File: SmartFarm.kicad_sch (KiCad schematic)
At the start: 30 parts, among them J1 Conn_01x20_Pin, J10 Conn_01x06_Socket, J11 Conn_01x06_Socket, J12 Conn_01x01_Pin, J13 Conn_01x01_Pin, J14 Conn_01x01_Pin, J15 Conn_01x01_Pin, J2 Conn_01x20_Pin, J3 Conn_01x06_Socket, J4 Conn_01x04, J5 Screw_Terminal_01x03, J6 Conn_01x01_Pin, J7 Screw_Terminal_01x03, J8 Barrel_Jack, J9 Screw_Terminal_01x03, SW1 SW_DIP_x01, SW2 SW_MEC_5E, SW3 SW_MEC_5E

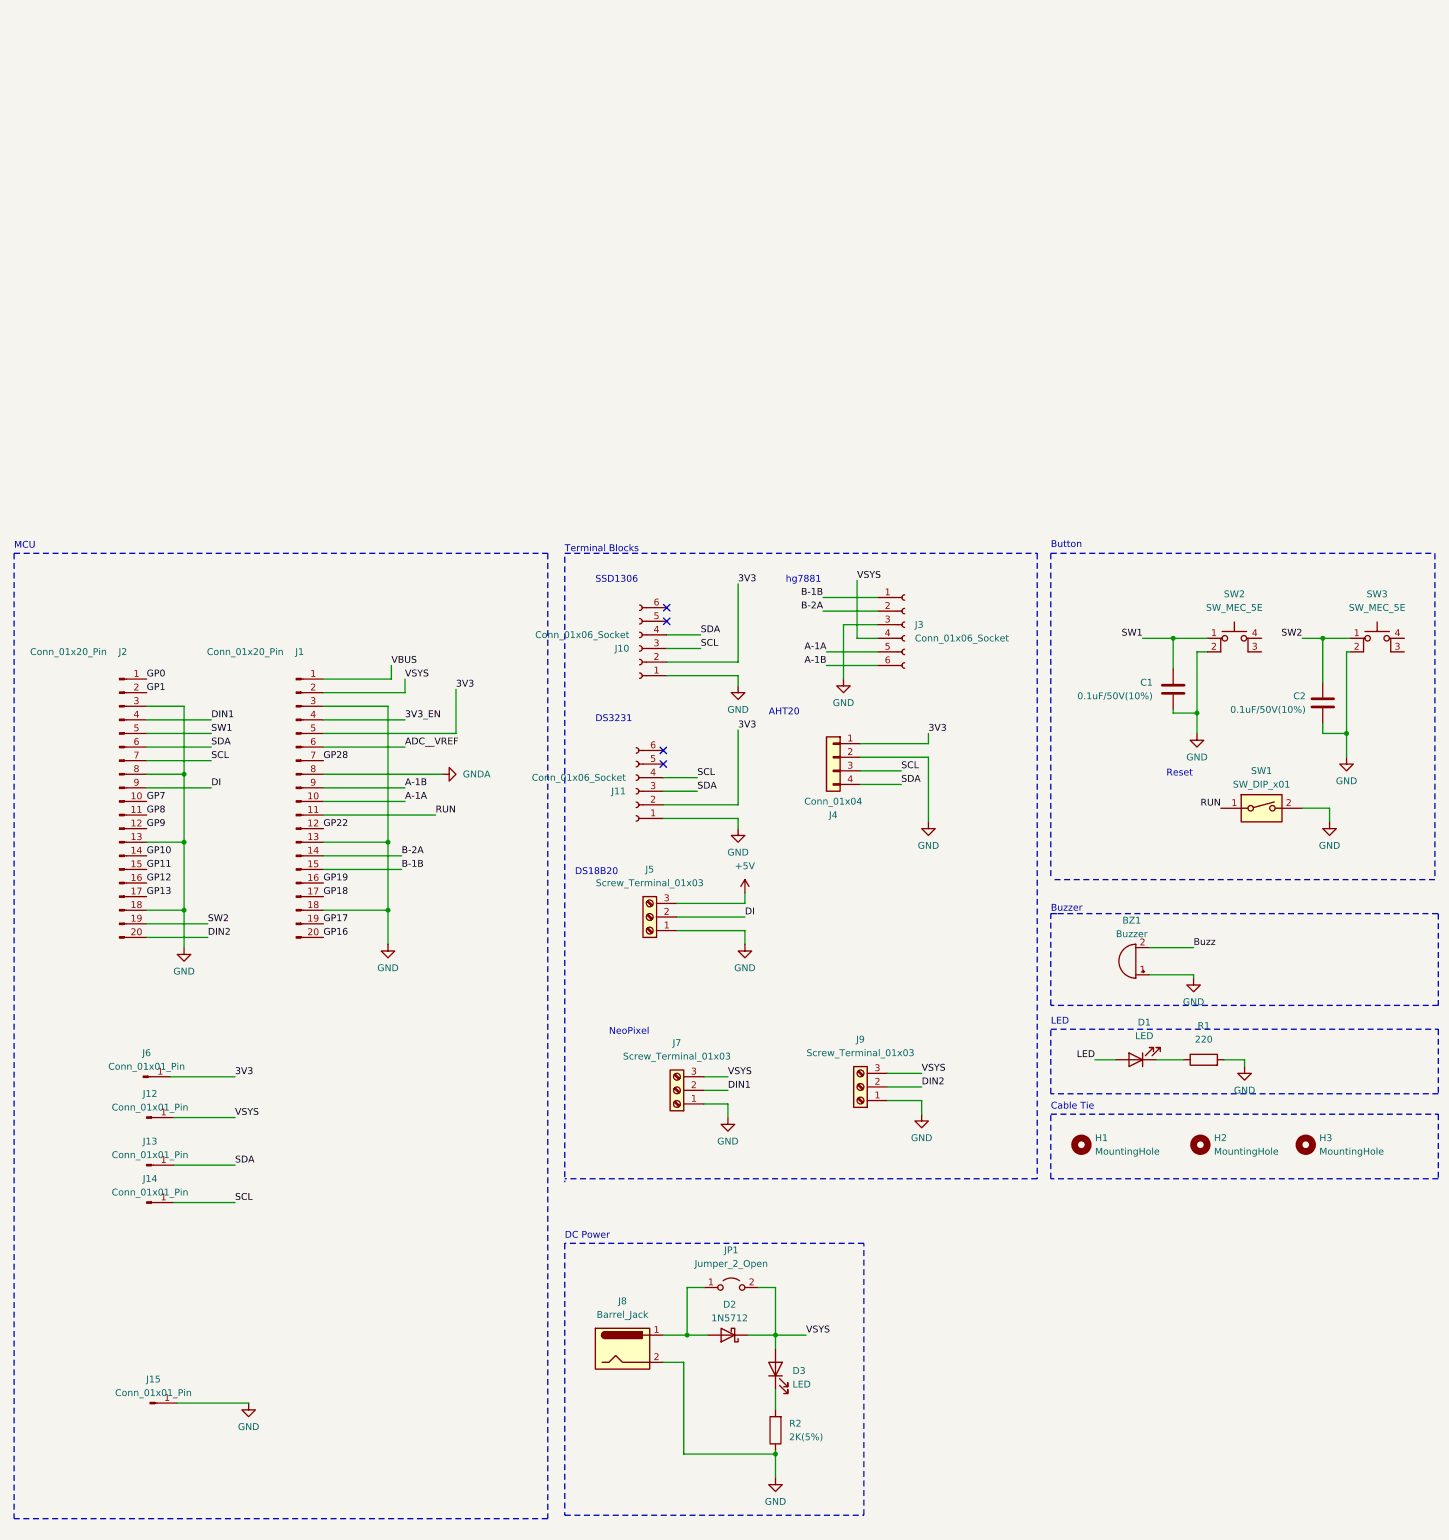
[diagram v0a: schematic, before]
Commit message: add potentialmeter and fan circuit
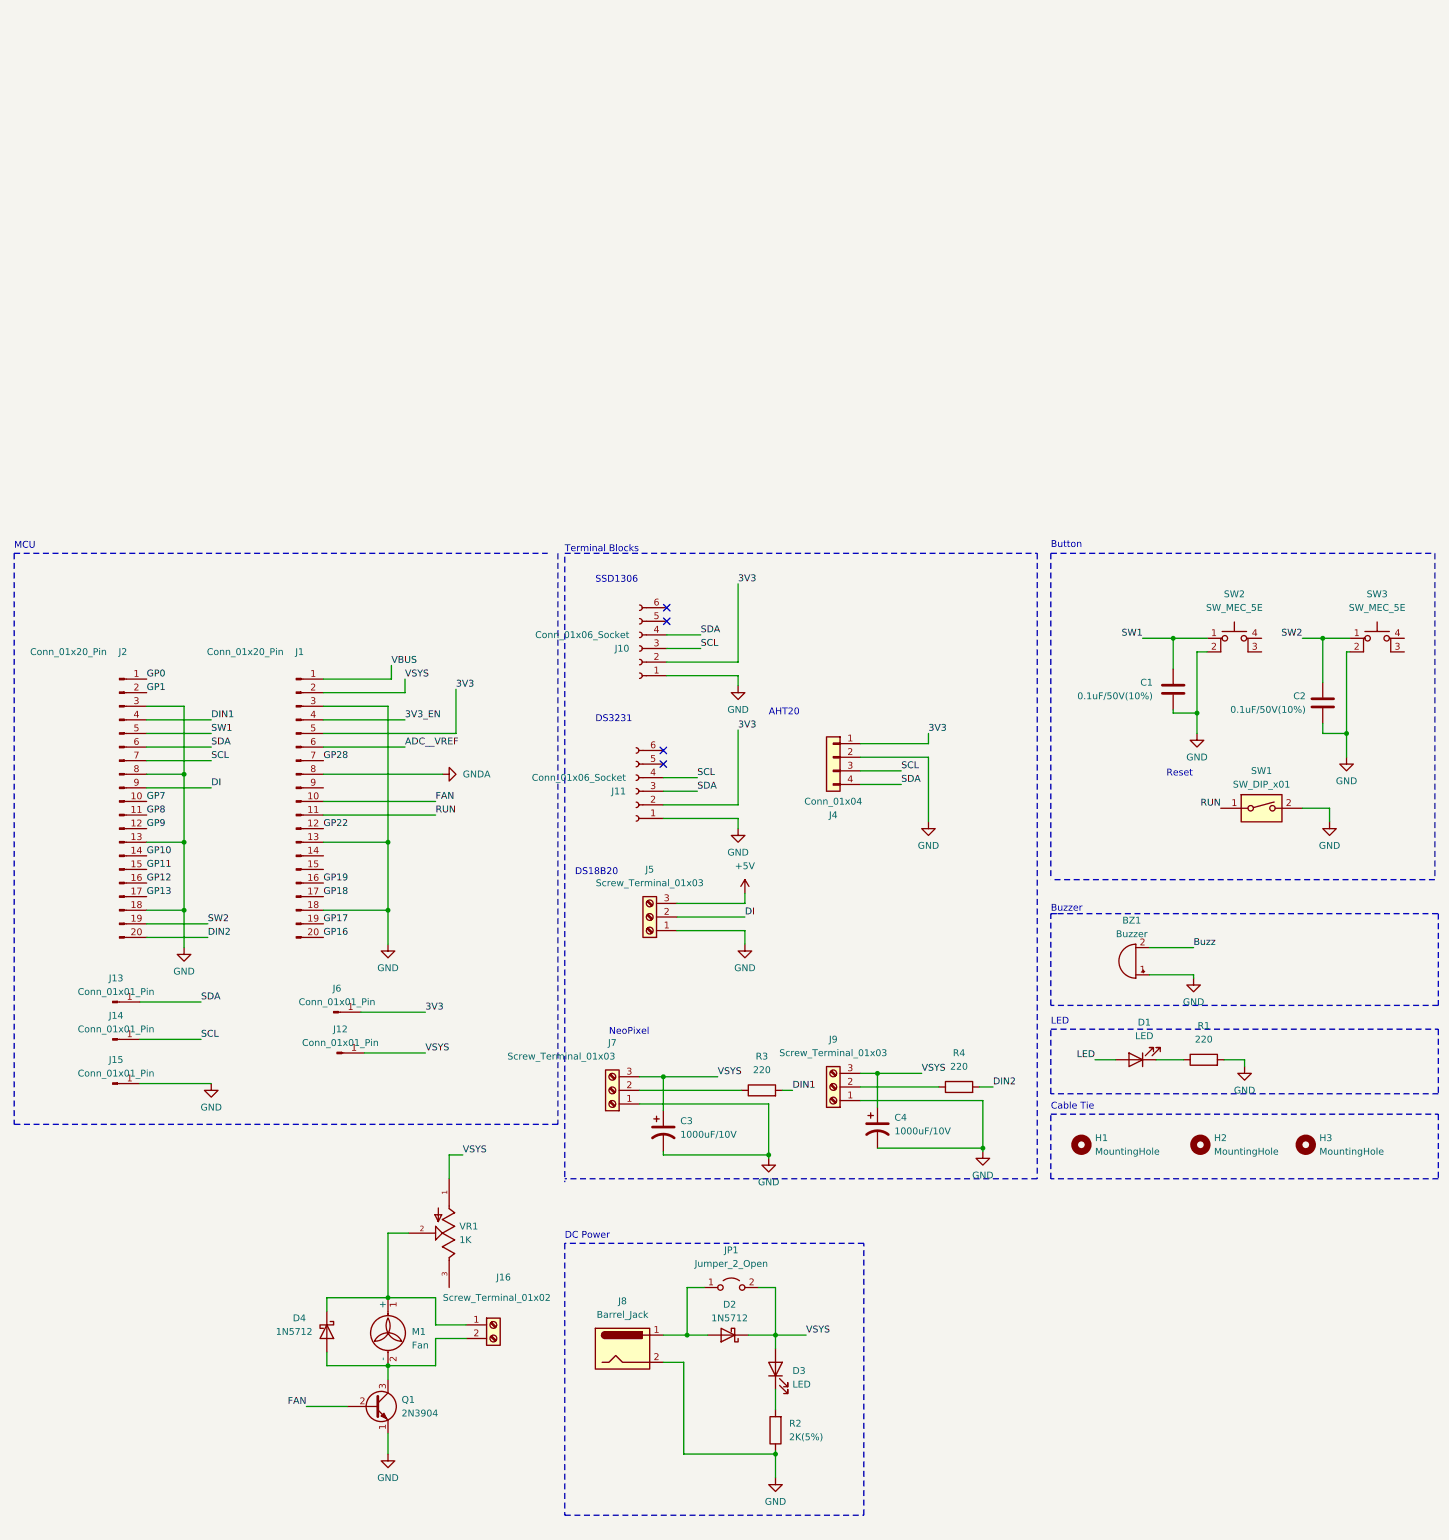
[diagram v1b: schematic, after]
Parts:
- removed J3: Conn_01x06_Socket, Connector_PinSocket_2.54mm:PinSocket_1x06_P2.54mm_Vertical, symbol Connector:Conn_01x06_Socket
- added C3, C4: 1000uF/10V, Capacitor_THT:CP_Radial_D8.0mm_P5.00mm, symbol Device:C_Polarized_US
- added D4: 1N5712, Diode_THT:D_DO-35_SOD27_P7.62mm_Horizontal, symbol Diode:1N5712
- added J16: Screw_Terminal_01x02, TerminalBlock_4Ucon:TerminalBlock_4Ucon_1x02_P3.50mm_Horizontal, symbol Connector:Screw_Terminal_01x02
- added M1: Fan, symbol Motor:Fan
- added Q1: 2N3904, Package_TO_SOT_THT:TO-92_Inline, symbol Transistor_BJT:2N3904
- added R3, R4: 220, Resistor_THT:R_Axial_DIN0204_L3.6mm_D1.6mm_P5.08mm_Horizontal, symbol Device:R
- added VR1: 1K, 3362P-1-103:TRIM_3362P-1-103, symbol 3362P-1-103:3362P-1-103
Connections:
- net DIN1: now also R3.2; no longer J7.2 (Pin_2)
- net DIN2: now also R4.2; no longer J9.2 (Pin_2)
- net GND: now also C3.2, C4.2, Q1.1 (E)
- net VSYS: now also C3.1, C4.1, VR1.1
- net A-1A renamed FAN
- net FAN: now also Q1.2 (B)
- net A-1B: no longer names the net of J1.9 (Pin_9)
- net B-1B: no longer names the net of J1.15 (Pin_15)
- net B-2A: no longer names the net of J1.14 (Pin_14)
- new net: J9.2 (Pin_2), R4.1
- new net: D4.1 (K), J16.1 (Pin_1), M1.1 (+), VR1.2
- new net: D4.2 (A), J16.2 (Pin_2), M1.2 (-), Q1.3 (C)
- new net: J7.2 (Pin_2), R3.1
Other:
- note removed: "hg7881"
- moved on the sheet: J12, J13, J14, J15, J6, J7, J9

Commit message: layout done
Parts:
- removed JP1: Jumper_2_Open, Jumper:SolderJumper-2_P1.3mm_Open_TrianglePad1.0x1.5mm, symbol Jumper:Jumper_2_Open
- added R5: 1k, Resistor_THT:R_Axial_DIN0204_L3.6mm_D1.6mm_P5.08mm_Horizontal, symbol Device:R
- added R6: 4.7k, Resistor_THT:R_Axial_DIN0204_L3.6mm_D1.6mm_P5.08mm_Horizontal, symbol Device:R
- D2, D4: footprint Diode_THT:D_DO-35_SOD27_P7.62mm_Horizontal -> Diode_THT:D_DO-35_SOD27_P10.16mm_Horizontal
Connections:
- net +5V is gone; now on net 3V3: J5.3 (Pin_3)
- net GP7 is gone; now on net Buzz: J2.10 (Pin_10)
- net GP9 is gone; now on net LED: J2.12 (Pin_12)
- net 3V3: now also R6.2
- net Buzz: now also BZ1.1 (-); no longer BZ1.2 (+)
- net DI: now also R6.1
- net FAN: now also R5.1; no longer Q1.2 (B)
- net GND: now also BZ1.2 (+); no longer BZ1.1 (-)
- new net: Q1.2 (B), R5.2
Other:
- moved on the sheet: BZ1, D4, J16, J5, M1, Q1, VR1

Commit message: sample
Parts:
- C3, C4: value 1000uF/10V -> 1000uF/6.3V
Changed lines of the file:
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@@
       (effects (font (size 1.27 1.27)) (justify left))
     )
-    (property "Value" "1000uF/10V" (at 178.435 123.825 0)
+    (property "Value" "1000uF/6.3V" (at 178.435 123.825 0)
       (effects (font (size 1.27 1.27)) (justify left))
     )
@@
       (effects (font (size 1.27 1.27)) hide)
     )
-    (property "Datasheet" "~" (at 175.26 123.19 0)
+    (property "Datasheet" "https://www.devicemart.co.kr/goods/download?id=14107&rank=1" (at 175.26 123.19 0)
       (effects (font (size 1.27 1.27)) hide)
     )
@@
       (effects (font (size 1.27 1.27)) (justify left))
     )
-    (property "Value" "1000uF/10V" (at 138.43 124.46 0)
+    (property "Value" "1000uF/6.3V" (at 138.43 124.46 0)
       (effects (font (size 1.27 1.27)) (justify left))
     )
@@
       (effects (font (size 1.27 1.27)) hide)
     )
-    (property "Datasheet" "~" (at 135.255 123.825 0)
-      (effects (font (size 1.27 1.27)) hide)
-    )
+    (property "Datasheet" "https://www.devicemart.co.kr/goods/download?id=14107&rank=1" (at 135.255 123.825 0)
+      (effects (font (size 1.27 1.27)) hide)
+    )
